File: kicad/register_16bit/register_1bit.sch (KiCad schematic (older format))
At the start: 3 parts

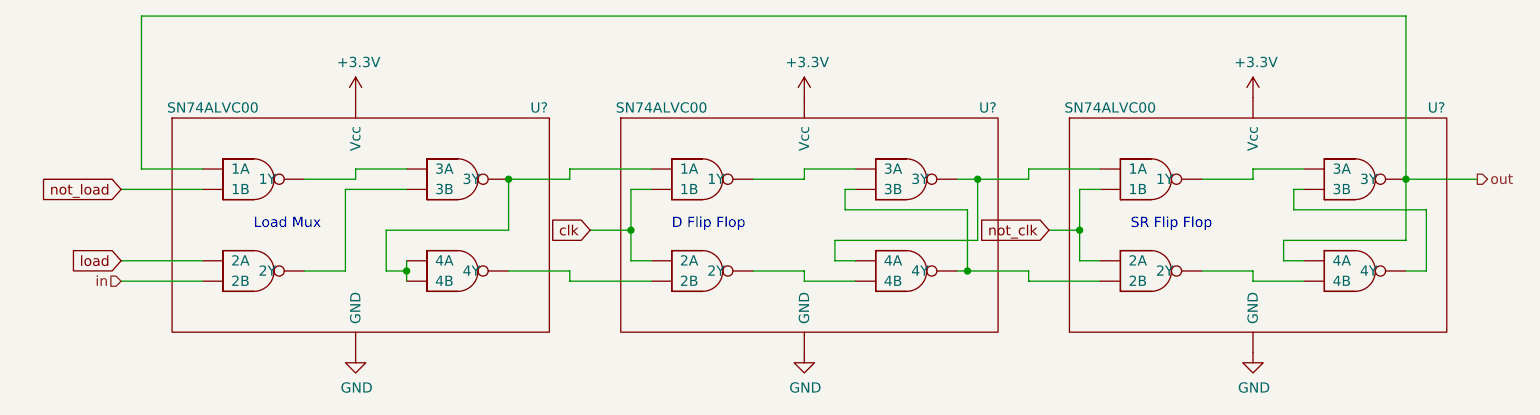
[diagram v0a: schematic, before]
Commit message: Finished initial PCB layout and routing for 16-bit register.
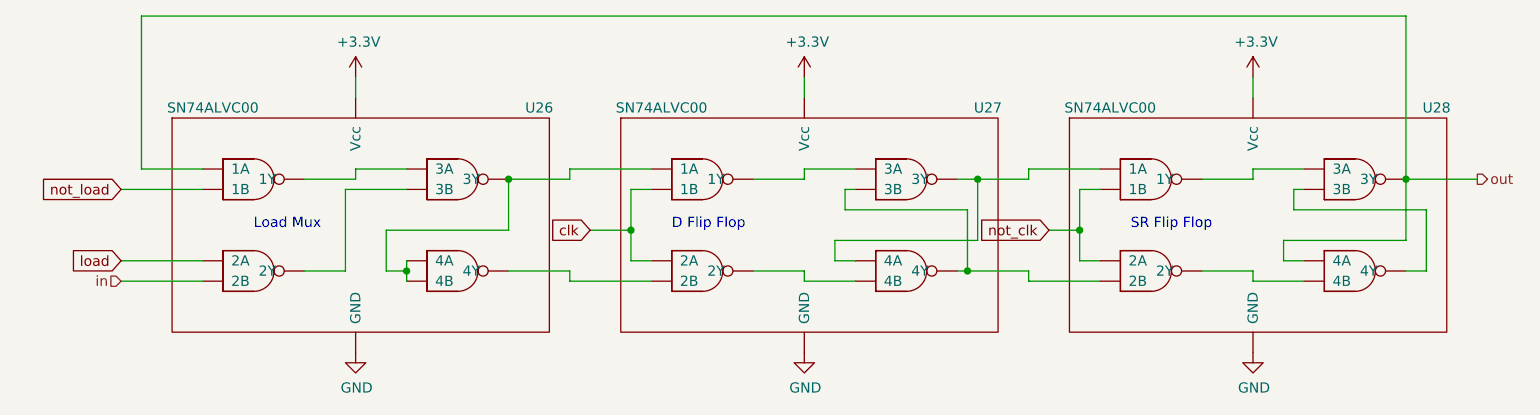
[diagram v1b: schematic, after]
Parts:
- gave numbers to parts that had none: 3

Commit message: ALU schematic, layout, routing complete. Associated motherboardmod. Also added Load LED to register and program counter boards.
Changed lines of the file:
@@
 AR Path="/5E6EC371/5E6EE94A" Ref="U41"  Part="1"
 AR Path="/5E6EC375/5E6EE94A" Ref="U44"  Part="1"
-F 0 "U26" H 4100 2600 50  0000 C CNN
+F 0 "U47" H 4100 2600 50  0000 C CNN
 F 1 "SN74ALVC00" H 2500 2600 50  0000 C CNN
 F 2 "Package_SO:TSSOP-14_4.4x5mm_P0.65mm" H 3200 1450 50  0001 C CNN
@@
 AR Path="/5E6EC371/5E6F4B7A" Ref="U42"  Part="1"
 AR Path="/5E6EC375/5E6F4B7A" Ref="U45"  Part="1"
-F 0 "U27" H 6300 2600 50  0000 C CNN
+F 0 "U48" H 6300 2600 50  0000 C CNN
 F 1 "SN74ALVC00" H 4700 2600 50  0000 C CNN
 F 2 "Package_SO:TSSOP-14_4.4x5mm_P0.65mm" H 5400 1450 50  0001 C CNN
@@
 AR Path="/5E6EC371/5E702849" Ref="U43"  Part="1"
 AR Path="/5E6EC375/5E702849" Ref="U46"  Part="1"
-F 0 "U28" H 8500 2600 50  0000 C CNN
+F 0 "U49" H 8500 2600 50  0000 C CNN
 F 1 "SN74ALVC00" H 6900 2600 50  0000 C CNN
 F 2 "Package_SO:TSSOP-14_4.4x5mm_P0.65mm" H 7600 1450 50  0001 C CNN

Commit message: Readme updates (#6)
* Readme intro section

* Board revisions for manufacturing, add digikey PNs to all, added logo.
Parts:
- U47, U48, U49: Digikey PN (none) -> 296-5104-1-ND
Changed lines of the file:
@@
 $Descr A4 11693 8268
 encoding utf-8
-Sheet 10 17
+Sheet 3 17
 Title "1-bit Register"
 Date "2020-03-15"
@@
 F 2 "Package_SO:TSSOP-14_4.4x5mm_P0.65mm" H 3200 1450 50  0001 C CNN
 F 3 "" H 3450 2950 50  0001 C CNN
+F 4 "296-5104-1-ND" H 0   0   50  0001 C CNN "Digikey PN"
 	1    3450 2950
 	1    0    0    -1
@@
 F 2 "Package_SO:TSSOP-14_4.4x5mm_P0.65mm" H 5400 1450 50  0001 C CNN
 F 3 "" H 5650 2950 50  0001 C CNN
+F 4 "296-5104-1-ND" H 0   0   50  0001 C CNN "Digikey PN"
 	1    5650 2950
 	1    0    0    -1
@@
 F 2 "Package_SO:TSSOP-14_4.4x5mm_P0.65mm" H 7600 1450 50  0001 C CNN
 F 3 "" H 7850 2950 50  0001 C CNN
+F 4 "296-5104-1-ND" H 0   0   50  0001 C CNN "Digikey PN"
 	1    7850 2950
 	1    0    0    -1
